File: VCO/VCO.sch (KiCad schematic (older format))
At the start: 21 parts, among them J1 JACK_STEREO, Q1 Q_NMOS_SGD, SW1 SWITCH_INV, U1 LM324

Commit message: Routage fait / petit défaut
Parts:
- removed H2: HEADER_DAC, Pin_Headers:Pin_Header_Straight_1x08_Pitch2.54mm, symbol CONN_01X08
- added H1: Header_left, Pin_Headers:Pin_Header_Straight_1x05_Pitch2.54mm, symbol CONN_01X05
- added H2: Header_right, Pin_Headers:Pin_Header_Straight_1x03_Pitch2.54mm, symbol CONN_01X03
- B1: renamed from H1; value HEADER_ALIM -> Bornier
- R2, R3, R4: value 50k -> 47k
- R5: value 100k -> 33k
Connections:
- net SCLK: now also H1.1 (P1)
- net SDI: now also H1.3 (P3)
- net SDO: now also H1.5 (P5)
- net ~ALERT: now also H2.3 (P3)
- net ~CLEAR: now also H2.2 (P2)
- net ~LDAC: now also H1.4 (P4)
- net ~RESET: now also H2.1 (P1)
- net ~SYNC: now also H1.2 (P2)
- net at C2.2, R5.2, R6.2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: now also U1.12 (+), U1.13 (-); no longer U1.5 (+), U1.6 (-)
- net at Q1.2 (G), R6.1, SW1.1: now also U1.14; no longer U1.7
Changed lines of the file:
@@
 P 4650 2650
 F 0 "R2" V 4730 2650 50  0000 C CNN
-F 1 "50k" V 4650 2650 50  0000 C CNN
+F 1 "47k" V 4650 2650 50  0000 C CNN
 F 2 "Resistors_ThroughHole:R_Axial_DIN0207_L6.3mm_D2.5mm_P7.62mm_Horizontal" V 4580 2650 50  0001 C CNN
 F 3 "" H 4650 2650 50  0000 C CNN
@@
 P 5150 3250
 F 0 "R3" V 5230 3250 50  0000 C CNN
-F 1 "50k" V 5150 3250 50  0000 C CNN
+F 1 "47k" V 5150 3250 50  0000 C CNN
 F 2 "Resistors_ThroughHole:R_Axial_DIN0207_L6.3mm_D2.5mm_P7.62mm_Horizontal" V 5080 3250 50  0001 C CNN
 F 3 "" H 5150 3250 50  0000 C CNN
@@
 P 6950 1900
 F 0 "R5" V 7030 1900 50  0000 C CNN
-F 1 "100k" V 6950 1900 50  0000 C CNN
+F 1 "33k" V 6950 1900 50  0000 C CNN
 F 2 "Resistors_ThroughHole:R_Axial_DIN0207_L6.3mm_D2.5mm_P7.62mm_Horizontal" V 6880 1900 50  0001 C CNN
 F 3 "" H 6950 1900 50  0000 C CNN
@@
 P 5400 3050
 F 0 "R4" V 5480 3050 50  0000 C CNN
-F 1 "50k" V 5400 3050 50  0000 C CNN
+F 1 "47k" V 5400 3050 50  0000 C CNN
 F 2 "Resistors_ThroughHole:R_Axial_DIN0207_L6.3mm_D2.5mm_P7.62mm_Horizontal" V 5330 3050 50  0001 C CNN
 F 3 "" H 5400 3050 50  0000 C CNN
@@
 $EndComp
 $Comp
-L CONN_01X03 H1
+L CONN_01X03 B1
 U 1 1 58E394FA
 P 4850 3350
-F 0 "H1" H 4850 3550 50  0000 C CNN
-F 1 "HEADER_ALIM" V 4950 3350 50  0000 C CNN
+F 0 "B1" H 4850 3550 50  0000 C CNN
+F 1 "Bornier" V 4950 3350 50  0000 C CNN
 F 2 "bornier:Bornier_3pins" H 4850 3350 50  0001 C CNN
 F 3 "" H 4850 3350 50  0000 C CNN
@@
 Text Label 2500 2400 2    60   ~ 0
 SDO
-Text Label 3850 1500 3    60   ~ 0
+Text Label 1900 2250 0    60   ~ 0
 SDO
 Text Label 2500 2550 2    60   ~ 0
 ~LDAC
-Text Label 3950 1500 3    60   ~ 0
+Text Label 1900 2350 0    60   ~ 0
 ~LDAC
 $Comp
@@
 Text Label 2500 2850 2    60   ~ 0
 ~SYNC
-Text Label 4050 1500 3    60   ~ 0
+Text Label 1900 2550 0    60   ~ 0
 ~SYNC
 Text Label 2500 3000 2    60   ~ 0
 SCLK
-Text Label 4150 1500 3    60   ~ 0
+Text Label 1900 2650 0    60   ~ 0
 SCLK
 Text Label 3500 3000 0    60   ~ 0
 ~RESET
-Text Label 4250 1500 3    60   ~ 0
+Text Label 3650 3800 1    60   ~ 0
 ~RESET
 Text Label 3500 3150 0    60   ~ 0
 ~CLEAR
-Text Label 4350 1500 3    60   ~ 0
+Text Label 3550 3800 1    60   ~ 0
 ~CLEAR
 Text Label 3500 3300 0    60   ~ 0
 ~ALERT
-Text Label 4450 1500 3    60   ~ 0
+Text Label 3450 3800 1    60   ~ 0
 ~ALERT
 $Comp
@@
 $Comp
 L LM324 U1
-U 2 1 58E7D0DD
+U 4 1 58E7D0DD
 P 7350 2650
 F 0 "U1" H 7400 2850 50  0000 C CNN
@@
 F 2 "Housings_DIP:DIP-14_W7.62mm" H 7300 2750 50  0001 C CNN
 F 3 "" H 7400 2850 50  0000 C CNN
-	2    7350 2650
-	1    0    0    -1
-$EndComp
-$Comp
-L CONN_01X08 H2
-U 1 1 58E8138D
-P 4200 1300
-F 0 "H2" H 4200 1750 50  0000 C CNN
-F 1 "HEADER_DAC" V 4300 1300 50  0000 C CNN
-F 2 "Pin_Headers:Pin_Header_Straight_1x08_Pitch2.54mm" H 4200 1300 50  0001 C CNN
-F 3 "" H 4200 1300 50  0000 C CNN
-	1    4200 1300
-	0    -1   -1   0
+	4    7350 2650
+	1    0    0    -1
 $EndComp
 Text Label 2500 2700 2    60   ~ 0
 SDI
-Text Label 4550 1500 3    60   ~ 0
+Text Label 1900 2450 0    60   ~ 0
 SDI
 $Comp
@@
 Wire Wire Line
 	9000 2350 9000 2200
+$Comp
+L CONN_01X05 H1
+U 1 1 58EFDB48
+P 1700 2450
+F 0 "H1" H 1700 2750 50  0000 C CNN
+F 1 "Header_left" V 1800 2450 50  0000 C CNN
+F 2 "Pin_Headers:Pin_Header_Straight_1x05_Pitch2.54mm" H 1700 2450 50  0001 C CNN
+F 3 "" H 1700 2450 50  0000 C CNN
+	1    1700 2450
+	-1   0    0    1
+$EndComp
+$Comp
+L CONN_01X03 H2
+U 1 1 58EFE144
+P 3550 4000
+F 0 "H2" H 3550 4200 50  0000 C CNN
+F 1 "Header_right" V 3650 4000 50  0000 C CNN
+F 2 "Pin_Headers:Pin_Header_Straight_1x03_Pitch2.54mm" H 3550 4000 50  0001 C CNN
+F 3 "" H 3550 4000 50  0000 C CNN
+	1    3550 4000
+	0    1    1    0
+$EndComp
 $EndSCHEMATC

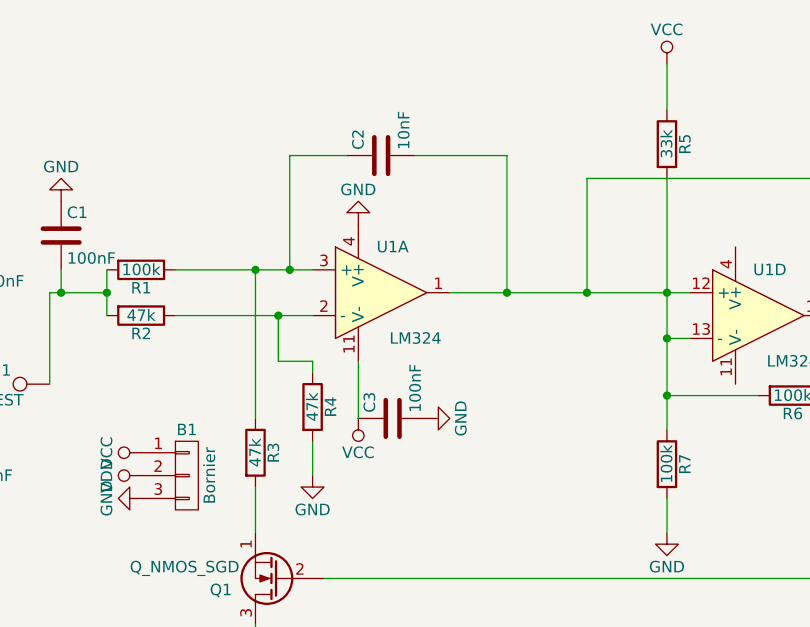
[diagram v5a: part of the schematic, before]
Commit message: Fixed AO power
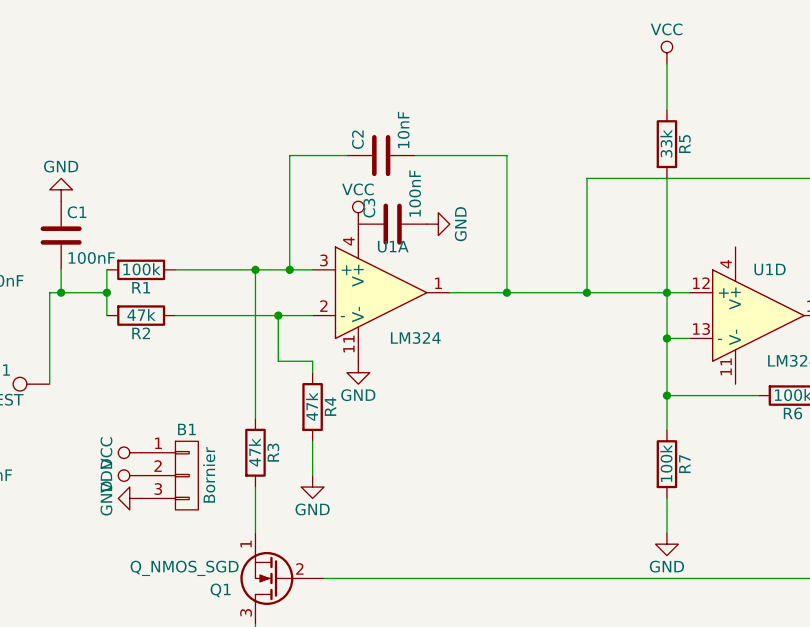
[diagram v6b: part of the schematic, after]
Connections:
- net GND: now also U1.11 (V-); no longer U1.4 (V+)
- net VCC: now also U1.4 (V+); no longer U1.11 (V-)
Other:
- moved on the sheet: C3
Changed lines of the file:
@@
 L C C3
 U 1 1 58BEDAEC
-P 5750 3100
-F 0 "C3" H 5775 3200 50  0000 L CNN
-F 1 "100nF" H 5775 3000 50  0000 L CNN
-F 2 "Capacitors_ThroughHole:C_Axial_L5.1mm_D3.1mm_P7.50mm_Horizontal" H 5788 2950 50  0001 C CNN
-F 3 "" H 5750 3100 50  0000 C CNN
-	1    5750 3100
+P 5750 2250
+F 0 "C3" H 5775 2350 50  0000 L CNN
+F 1 "100nF" H 5775 2150 50  0000 L CNN
+F 2 "Capacitors_ThroughHole:C_Axial_L5.1mm_D3.1mm_P7.50mm_Horizontal" H 5788 2100 50  0001 C CNN
+F 3 "" H 5750 2250 50  0000 C CNN
+	1    5750 2250
 	0    -1   -1   0
 $EndComp
@@
 L GND #PWR05
 U 1 1 58C825A1
-P 5600 2250
-F 0 "#PWR05" H 5600 2000 50  0001 C CNN
-F 1 "GND" H 5600 2100 50  0000 C CNN
-F 2 "" H 5600 2250 50  0000 C CNN
-F 3 "" H 5600 2250 50  0000 C CNN
-	1    5600 2250
-	-1   0    0    1
+P 5600 2850
+F 0 "#PWR05" H 5600 2600 50  0001 C CNN
+F 1 "GND" H 5600 2700 50  0000 C CNN
+F 2 "" H 5600 2850 50  0000 C CNN
+F 3 "" H 5600 2850 50  0000 C CNN
+	1    5600 2850
+	1    0    0    -1
 $EndComp
 $Comp
@@
 L GND #PWR07
 U 1 1 58C856DC
-P 5900 3100
-F 0 "#PWR07" H 5900 2850 50  0001 C CNN
-F 1 "GND" H 5900 2950 50  0000 C CNN
-F 2 "" H 5900 3100 50  0000 C CNN
-F 3 "" H 5900 3100 50  0000 C CNN
-	1    5900 3100
+P 5900 2250
+F 0 "#PWR07" H 5900 2000 50  0001 C CNN
+F 1 "GND" H 5900 2100 50  0000 C CNN
+F 2 "" H 5900 2250 50  0000 C CNN
+F 3 "" H 5900 2250 50  0000 C CNN
+	1    5900 2250
 	0    -1   -1   0
 $EndComp
@@
 L VCC #PWR013
 U 1 1 58DA723D
-P 5600 3100
-F 0 "#PWR013" H 5600 2950 50  0001 C CNN
-F 1 "VCC" H 5600 3250 50  0000 C CNN
-F 2 "" H 5600 3100 50  0000 C CNN
-F 3 "" H 5600 3100 50  0000 C CNN
-	1    5600 3100
-	-1   0    0    1
+P 5600 2250
+F 0 "#PWR013" H 5600 2100 50  0001 C CNN
+F 1 "VCC" H 5600 2400 50  0000 C CNN
+F 2 "" H 5600 2250 50  0000 C CNN
+F 3 "" H 5600 2250 50  0000 C CNN
+	1    5600 2250
+	1    0    0    -1
 $EndComp
 $Comp
@@
 	6000 2550 7050 2550
 Wire Wire Line
-	5600 2850 5600 3100
-Wire Wire Line
 	4500 2550 4250 2550
